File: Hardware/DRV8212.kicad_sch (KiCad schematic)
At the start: 19 parts, among them J12 Screw_Terminal_01x02, U24 DRV8870DDA, U25 SN74LVC1G00DBV, U26 SN74LVC1G00DBV, U7 INA219AxDCN

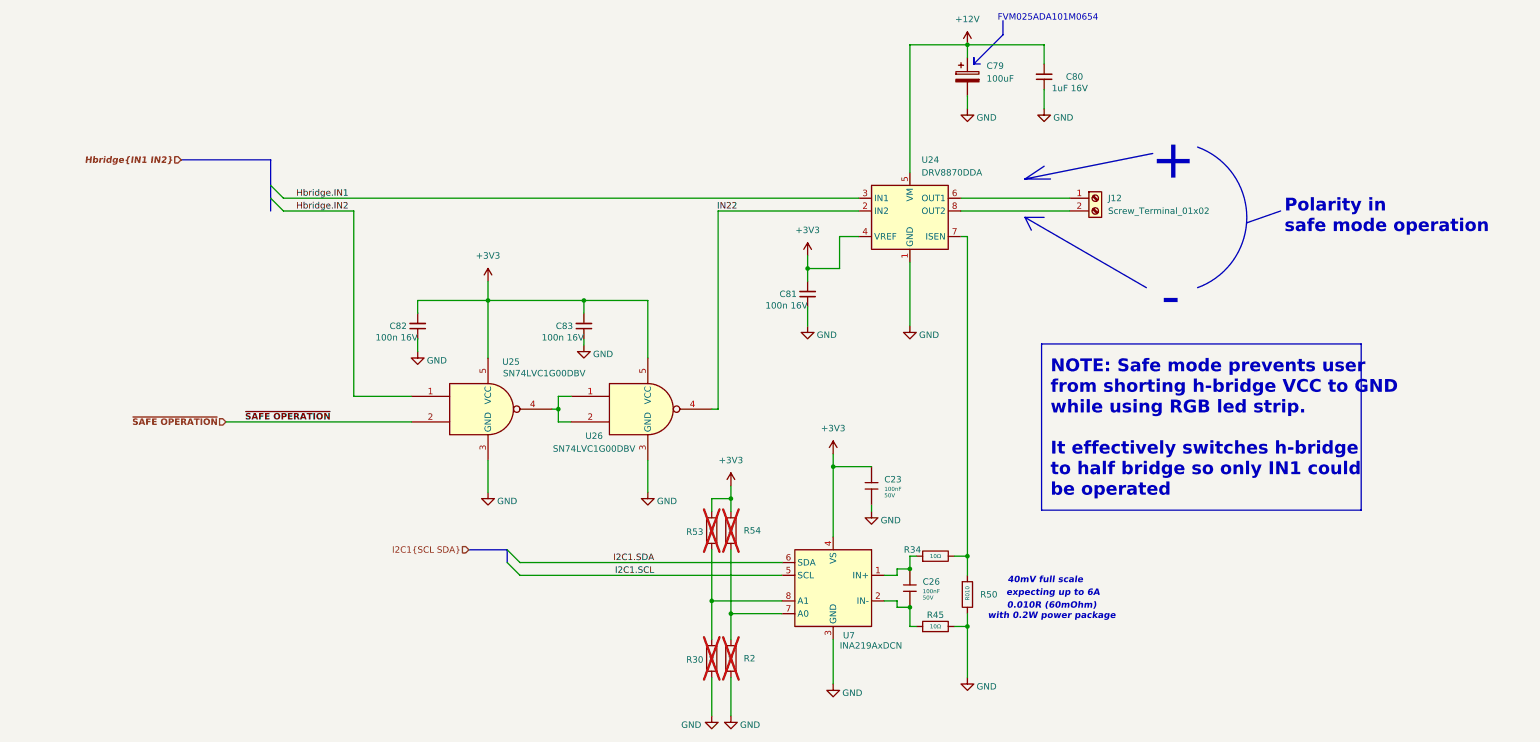
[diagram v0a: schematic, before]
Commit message: Fix INA layout
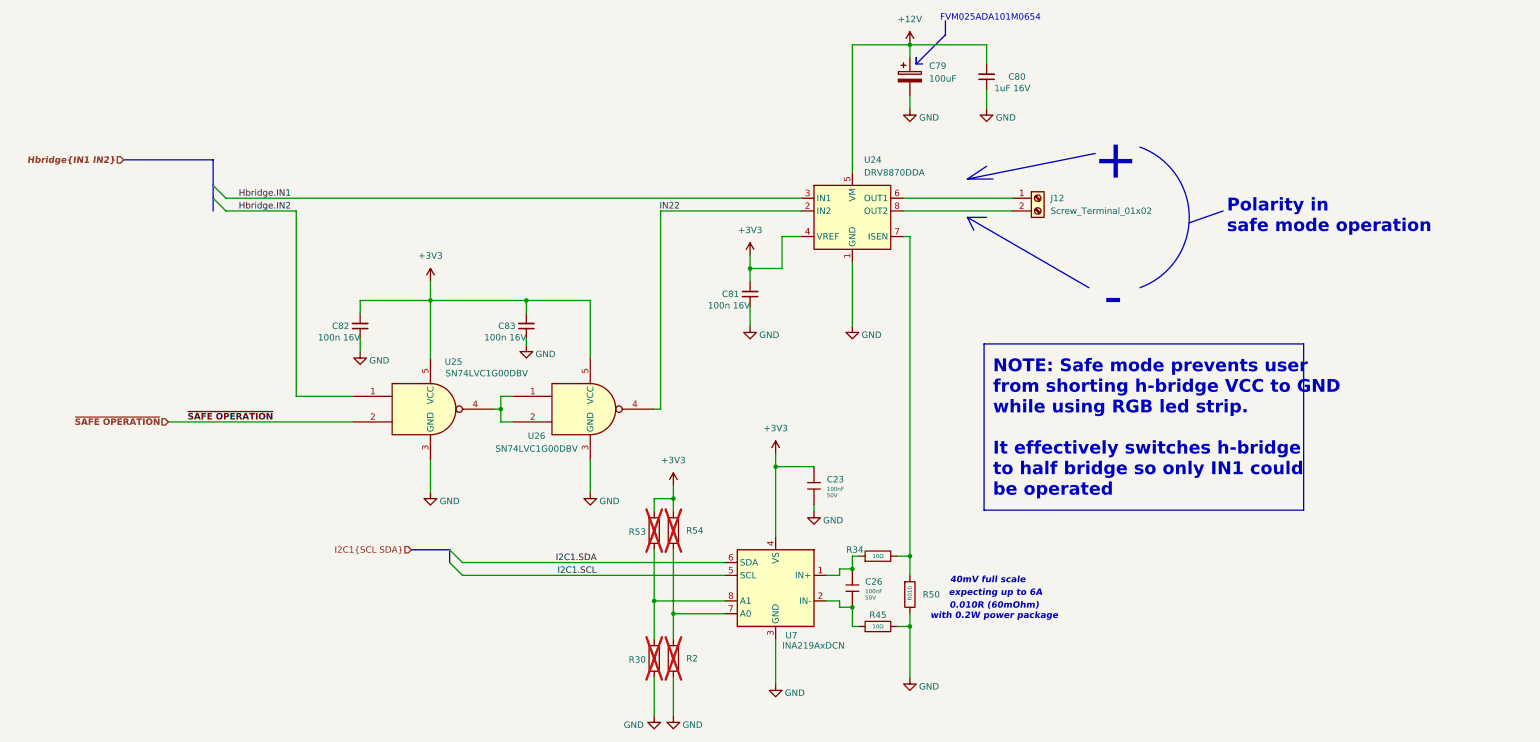
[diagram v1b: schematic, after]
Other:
- moved on the sheet: C23, C26, C79, C80, C81, C82, C83, J12, R2, R30, R34, R45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

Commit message: Add BOM+CPL
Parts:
- C80: value 1uF 16V -> 100nF
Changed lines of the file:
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@@
 			)
 		)
-		(property "Value" "1uF 16V"
+		(property "Value" "100nF"
 			(at 200.914 39.116 0)
 			(effects
@@
 		(on_board yes)
 		(dnp no)
-		(fields_autoplaced yes)
 		(property "Reference" "#PWR0170"
 			(at 152.4 76.2 0)
